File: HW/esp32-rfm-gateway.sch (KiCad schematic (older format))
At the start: 46 parts, among them J1 PinsI2C, J2 PinDbg, J20 MicroUSB-B, J3 PinsGP, J30 Ant, Q20 IRLML2244, SW1 BootBtn, U1 ESP-WROOM-32, U2 BD48K30, U20 MCP73831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

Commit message: Positions the components, almost ...
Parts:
- removed BT1: LiIon, CalinConnectors:BattHolder-AA-PCB, symbol calin:BATTERY
- removed J20: MicroUSB-B, CalinConnectors:USB-MicroB-10118194-0x0, symbol calin:MicroUSB-B
- removed J3: PinsGP, CalinConnectors:Pin_Header_Straight_1x07, symbol calin:CS_7
- removed J30: Ant, CalinConnectors:U.FL, symbol calin:CS_4
- removed SW1: BootBtn, CalinGeneric:SW-Push-4, symbol calin:SW-Push4
- added C5: 100nF, CalinGeneric:C0805HS, symbol Device:C
- added H3, H4: Hole, CalinGeneric:HoleNPT-M3, symbol calin:Hole
- added J1: Res, CalinConnectors:Pin_Header_Straight_1x02, symbol calin:CS_2
- added J2: Boot, CalinConnectors:Pin_Header_Straight_1x02, symbol calin:CS_2
- added J20: 220 V~, CalinConnectors:DG301-5-2, symbol calin:CS_2s
- added J21: c5V, CalinConnectors:Pin_Header_Straight_1x02, symbol calin:CS_2s
- added J22: s14500, CalinConnectors:BattHolder-AA-PCB, symbol calin:CS_2
- added J23: s18650, CalinConnectors:KEYS-1043, symbol calin:CS_2
- added J30: AntSMA, CalinConnectors:SMA-90, symbol calin:CS_5
- added SYM3: High Voltage !, Symbol:Symbol_HighVoltage_Type1_CopperTop_Big, symbol calin:Symbol_Generic
- added U24: IRM-05, CalinGeneric:IRM222A, symbol calin:IRM-05
- J3: renamed from J2; footprint CalinConnectors:Pin_Header_Straight_1x03 -> CalinConnectors:Pin_Header_Straight_1x03_Cyan
- renumbered J1 to J4
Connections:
- wire segments 195 -> 196
- no-connect marks 14 -> 22
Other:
- note removed: "1. Doar cu G738/G706: IRM-10-5 ca sursa de alimentare, dispare conectorul microUSB, sau pur si simplu ramane ca optional !\n2. Suport pt baterie 18650\n3. Modulul ESP32 trebuie in dreapta sus cum e in PCB acum !"
- moved on the sheet: C1, C20, C21, D20, R20, R21, U20

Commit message: Changes NPTH holes and adds 3 pin AC connector
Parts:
- removed J20: 220 V~, CalinConnectors:DG301-5-2, symbol calin:CS_2s
- added J20: 220V~, CalinConnectors:DG301-5-3, symbol calin:CS_3
- H1, H2, H3, H4: footprint CalinGeneric:HoleNPT-M3 -> CalinGeneric:HoleNPT-M2.5
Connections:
- net labels added: ACE, ACL, ACN, Earth
- wire segments 196 -> 194
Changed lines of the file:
@@
 F 0 "H1" H 10128 850 60  0000 L CNN
 F 1 "Hole" H 10150 800 60  0001 C CNN
-F 2 "CalinGeneric:HoleNPT-M3" H 10050 850 60  0001 C CNN
+F 2 "CalinGeneric:HoleNPT-M2.5" H 10050 850 60  0001 C CNN
 F 3 "" H 10050 850 60  0000 C CNN
 	1    10050 850
@@
 F 0 "H2" H 10628 850 60  0000 L CNN
 F 1 "Hole" H 10650 800 60  0001 C CNN
-F 2 "CalinGeneric:HoleNPT-M3" H 10550 850 60  0001 C CNN
+F 2 "CalinGeneric:HoleNPT-M2.5" H 10550 850 60  0001 C CNN
 F 3 "" H 10550 850 60  0000 C CNN
 	1    10550 850
@@
 PwrSW
 $Comp
-L calin:CS_2s J20
-U 1 1 5CAC0659
-P 1250 6850
-F 0 "J20" V 1350 6850 60  0000 C CNN
-F 1 "220 V~" H 1250 7000 50  0000 C CNN
-F 2 "CalinConnectors:DG301-5-2" H 1250 6900 60  0001 C CNN
-F 3 "" H 1250 6900 60  0000 C CNN
-	1    1250 6850
-	-1   0    0    -1
-$EndComp
-$Comp
 L calin:IRM-05 U24
 U 1 1 5CACF244
@@
 Wire Wire Line
 	2500 6950 2400 6950
-Wire Wire Line
-	1400 6800 1500 6800
-Wire Wire Line
-	1500 6800 1500 6750
-Wire Wire Line
-	1500 6750 1600 6750
-Wire Wire Line
-	1400 6900 1500 6900
-Wire Wire Line
-	1500 6900 1500 6950
-Wire Wire Line
-	1500 6950 1600 6950
 $Comp
 L calin:CS_2s J21
@@
 L calin:Symbol_Generic SYM3
 U 1 1 5CB3E766
-P 1050 6550
-F 0 "SYM3" H 1200 6550 50  0001 C CNN
-F 1 "High Voltage !" H 1128 6550 50  0000 L CNN
-F 2 "Symbol:Symbol_HighVoltage_Type1_CopperTop_Big" H 1050 6550 50  0001 C CNN
-F 3 "" V 1050 6550 50  0001 C CNN
-	1    1050 6550
+P 1050 6350
+F 0 "SYM3" H 1200 6350 50  0001 C CNN
+F 1 "High Voltage !" H 1128 6350 50  0000 L CNN
+F 2 "Symbol:Symbol_HighVoltage_Type1_CopperTop_Big" H 1050 6350 50  0001 C CNN
+F 3 "" V 1050 6350 50  0001 C CNN
+	1    1050 6350
 	1    0    0    -1
 $EndComp
@@
 F 0 "H3" H 10128 1050 60  0000 L CNN
 F 1 "Hole" H 10150 1000 60  0001 C CNN
-F 2 "CalinGeneric:HoleNPT-M3" H 10050 1050 60  0001 C CNN
+F 2 "CalinGeneric:HoleNPT-M2.5" H 10050 1050 60  0001 C CNN
 F 3 "" H 10050 1050 60  0000 C CNN
 	1    10050 1050
@@
 F 0 "H4" H 10628 1050 60  0000 L CNN
 F 1 "Hole" H 10650 1000 60  0001 C CNN
-F 2 "CalinGeneric:HoleNPT-M3" H 10550 1050 60  0001 C CNN
+F 2 "CalinGeneric:HoleNPT-M2.5" H 10550 1050 60  0001 C CNN
 F 3 "" H 10550 1050 60  0000 C CNN
 	1    10550 1050
@@
 	5750 5400 5750 4900
 Connection ~ 5750 5400
+$Comp
+L calin:CS_3 J20
+U 1 1 5CAC2EE6
+P 1050 6850
+F 0 "J20" V 1150 6850 60  0000 C CNN
+F 1 "220V~" H 1050 6650 50  0000 C CNN
+F 2 "CalinConnectors:DG301-5-3" H 1050 6950 60  0001 C CNN
+F 3 "" H 1050 6950 60  0000 C CNN
+	1    1050 6850
+	-1   0    0    1
+$EndComp
+$Comp
+L power:Earth #PWR0141
+U 1 1 5CAEA74F
+P 1500 7050
+F 0 "#PWR0141" H 1500 6800 50  0001 C CNN
+F 1 "Earth" H 1500 6900 50  0001 C CNN
+F 2 "" H 1500 7050 50  0001 C CNN
+F 3 "~" H 1500 7050 50  0001 C CNN
+	1    1500 7050
+	1    0    0    -1
+$EndComp
+Wire Wire Line
+	1200 6750 1600 6750
+Wire Wire Line
+	1200 6950 1600 6950
+Wire Wire Line
+	1500 6850 1500 7050
+Wire Wire Line
+	1200 6850 1500 6850
+Text Label 1250 6750 0    50   ~ 0
+ACL
+Text Label 1250 6850 0    50   ~ 0
+ACE
+Text Label 1250 6950 0    50   ~ 0
+ACN
 $EndSCHEMATC

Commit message: Creates an Earth plane
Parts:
- SYM3: footprint Symbol:Symbol_HighVoltage_Type1_CopperTop_Big -> Symbol:Symbol_Highvoltage_Type2_CopperTop_Small
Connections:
- net labels removed: ACE
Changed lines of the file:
@@
 Title "ESP32 RFM69/RFM9x Gateway"
 Date "2019-04-08"
-Rev "6"
+Rev "7"
 Comp "Calin Radoni"
 Comment1 ""
@@
 F 0 "SYM3" H 1200 6350 50  0001 C CNN
 F 1 "High Voltage !" H 1128 6350 50  0000 L CNN
-F 2 "Symbol:Symbol_HighVoltage_Type1_CopperTop_Big" H 1050 6350 50  0001 C CNN
+F 2 "Symbol:Symbol_Highvoltage_Type2_CopperTop_Small" H 1050 6350 50  0001 C CNN
 F 3 "" V 1050 6350 50  0001 C CNN
 	1    1050 6350
@@
 	-1   0    0    1
 $EndComp
+Wire Wire Line
+	1200 6750 1600 6750
+Wire Wire Line
+	1200 6950 1600 6950
+Wire Wire Line
+	1500 6850 1500 7050
+Wire Wire Line
+	1200 6850 1500 6850
+Text Label 1300 6750 0    50   ~ 0
+ACL
+Text Label 1300 6950 0    50   ~ 0
+ACN
 $Comp
 L power:Earth #PWR0141
-U 1 1 5CAEA74F
+U 1 1 5CB3D39A
 P 1500 7050
 F 0 "#PWR0141" H 1500 6800 50  0001 C CNN
@@
 	1    0    0    -1
 $EndComp
-Wire Wire Line
-	1200 6750 1600 6750
-Wire Wire Line
-	1200 6950 1600 6950
-Wire Wire Line
-	1500 6850 1500 7050
-Wire Wire Line
-	1200 6850 1500 6850
-Text Label 1250 6750 0    50   ~ 0
-ACL
 Text Label 1250 6850 0    50   ~ 0
-ACE
-Text Label 1250 6950 0    50   ~ 0
-ACN
+Earth
 $EndSCHEMATC

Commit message: The layout is established
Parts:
- added J5: PinsI2C, CalinConnectors:Pin_Header_Straight_1x04, symbol calin:CS_4
- added SYM4: High Voltage !, Symbol:Symbol_HighVoltage_Type1_CopperTop_Big, symbol calin:Symbol_Generic
- SYM3: footprint Symbol:Symbol_Highvoltage_Type2_CopperTop_Small -> Symbol:Symbol_HighVoltage_Type1_CopperTop_Big
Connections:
- wire segments 194 -> 198
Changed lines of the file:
@@
 Sheet 1 1
 Title "ESP32 RFM69/RFM9x Gateway"
-Date "2019-04-08"
-Rev "7"
+Date "2019-04-09"
+Rev "9"
 Comp "Calin Radoni"
 Comment1 ""
@@
 F 0 "SYM3" H 1200 6350 50  0001 C CNN
 F 1 "High Voltage !" H 1128 6350 50  0000 L CNN
-F 2 "Symbol:Symbol_Highvoltage_Type2_CopperTop_Small" H 1050 6350 50  0001 C CNN
+F 2 "Symbol:Symbol_HighVoltage_Type1_CopperTop_Big" H 1050 6350 50  0001 C CNN
 F 3 "" V 1050 6350 50  0001 C CNN
 	1    1050 6350
@@
 Text Label 1250 6850 0    50   ~ 0
 Earth
+$Comp
+L calin:Symbol_Generic SYM4
+U 1 1 5CAC5E73
+P 1050 6500
+F 0 "SYM4" H 1200 6500 50  0001 C CNN
+F 1 "High Voltage !" H 1128 6500 50  0000 L CNN
+F 2 "Symbol:Symbol_HighVoltage_Type1_CopperTop_Big" H 1050 6500 50  0001 C CNN
+F 3 "" V 1050 6500 50  0001 C CNN
+	1    1050 6500
+	1    0    0    -1
+$EndComp
+$Comp
+L calin:CS_4 J5
+U 1 1 5CAE5A37
+P 8200 1100
+F 0 "J5" H 8200 1350 60  0000 C CNN
+F 1 "PinsI2C" V 8300 1100 50  0000 C CNN
+F 2 "CalinConnectors:Pin_Header_Straight_1x04" H 8200 1250 60  0001 C CNN
+F 3 "" H 8200 1250 60  0000 C CNN
+	1    8200 1100
+	1    0    0    -1
+$EndComp
+$Comp
+L power:GND #PWR0142
+U 1 1 5CAE5A3D
+P 7950 1050
+F 0 "#PWR0142" H 7950 800 50  0001 C CNN
+F 1 "GND" V 7950 850 50  0000 C CNN
+F 2 "" H 7950 1050 50  0000 C CNN
+F 3 "" H 7950 1050 50  0000 C CNN
+	1    7950 1050
+	0    1    1    0
+$EndComp
+$Comp
+L power:+3V3 #PWR0143
+U 1 1 5CAE5A43
+P 7950 950
+F 0 "#PWR0143" H 7950 800 50  0001 C CNN
+F 1 "+3V3" V 7950 1150 50  0000 C CNN
+F 2 "" H 7950 950 50  0000 C CNN
+F 3 "" H 7950 950 50  0000 C CNN
+	1    7950 950
+	0    -1   -1   0
+$EndComp
+Wire Wire Line
+	8050 950  7950 950
+Wire Wire Line
+	8050 1050 7950 1050
+Wire Wire Line
+	8050 1150 7550 1150
+Wire Wire Line
+	8050 1250 7550 1250
+Text Label 7650 1150 0    50   ~ 0
+SCL
+Text Label 7650 1250 0    50   ~ 0
+SDA
 $EndSCHEMATC

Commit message: The margins are established
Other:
- note added: "1. MCP73832T-2ACI (sau 2ADI) pentru ca are Stat open-drain\n2. Split R25 ca sa vezi daca 5V e prezenta sau NU"
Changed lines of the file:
@@
 Text Label 7650 1250 0    50   ~ 0
 SDA
+Text Notes 4300 4200 0    118  ~ 0
+1. MCP73832T-2ACI (sau 2ADI) pentru ca are Stat open-drain\n2. Split R25 ca sa vezi daca 5V e prezenta sau NU
 $EndSCHEMATC

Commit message: Changes the power supply to provide stats, to a better annotation and to comply with ERC checks
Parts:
- added R26: 10k, CalinGeneric:R0805HS, symbol calin:R
- R21: value 1K -> 330
- U21: renamed from U20; value MCP73831 -> MCP73832T-2ACI
- renumbered R26 to R27, R27 to R28, U24 to U20, U21 to U24
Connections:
- net labels added: ADC_Vin, ChargeStat
- net labels removed: ADCIN, VinBOR
- wire segments 198 -> 207
- no-connect marks 22 -> 21
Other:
- note removed: "1. MCP73832T-2ACI (sau 2ADI) pentru ca are Stat open-drain\n2. Split R25 ca sa vezi daca 5V e prezenta sau NU"
- moved on the sheet: C22, C23, C24, C5, D21, J21, L21, Q20, R22, R23, R24, R25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

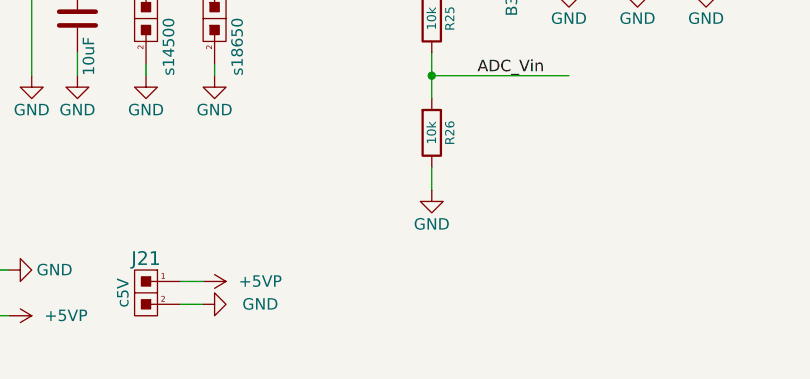
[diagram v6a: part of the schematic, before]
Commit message: Adds a new 5V header to be placed as placeholder in the power section
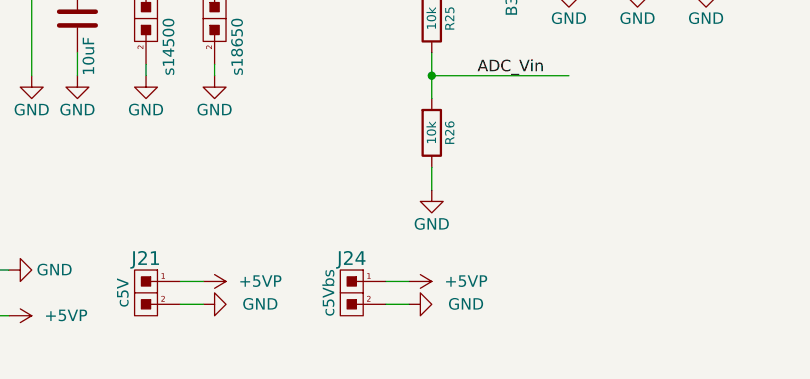
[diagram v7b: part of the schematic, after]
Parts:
- added J24: c5Vbs, CalinConnectors:Pin_Header_Angled_1x02, symbol calin:CS_2s
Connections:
- wire segments 207 -> 209
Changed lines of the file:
@@
 Sheet 1 1
 Title "ESP32 RFM69/RFM9x Gateway"
-Date "2019-04-09"
-Rev "9"
+Date "2019-04-13"
+Rev "10"
 Comp "Calin Radoni"
 Comment1 ""
@@
 	6450 4900 5600 4900
 $Comp
-L power:PWR_FLAG #FLG?
+L power:PWR_FLAG #FLG0104
 U 1 1 5CC8F59E
 P 1550 6850
-F 0 "#FLG?" H 1550 6925 50  0001 C CNN
+F 0 "#FLG0104" H 1550 6925 50  0001 C CNN
 F 1 "PWR_FLAG" V 1500 6950 20  0000 C CNN
 F 2 "" H 1550 6850 50  0001 C CNN
@@
 	1550 6850 1500 6850
 Connection ~ 1500 6850
+$Comp
+L calin:CS_2s J24
+U 1 1 5CB25633
+P 4050 6850
+F 0 "J24" H 4050 7000 60  0000 C CNN
+F 1 "c5Vbs" V 4150 6850 50  0000 C CNN
+F 2 "CalinConnectors:Pin_Header_Angled_1x02" H 4050 6900 60  0001 C CNN
+F 3 "" H 4050 6900 60  0000 C CNN
+	1    4050 6850
+	-1   0    0    -1
+$EndComp
+$Comp
+L power:+5VP #PWR0144
+U 1 1 5CB25639
+P 4300 6800
+F 0 "#PWR0144" H 4300 6650 50  0001 C CNN
+F 1 "+5VP" V 4300 7050 50  0000 C CNN
+F 2 "" H 4300 6800 50  0000 C CNN
+F 3 "" H 4300 6800 50  0000 C CNN
+	1    4300 6800
+	0    1    1    0
+$EndComp
+$Comp
+L power:GND #PWR0145
+U 1 1 5CB2563F
+P 4300 6900
+F 0 "#PWR0145" H 4300 6650 50  0001 C CNN
+F 1 "GND" V 4300 6650 50  0000 C CNN
+F 2 "" H 4300 6900 50  0000 C CNN
+F 3 "" H 4300 6900 50  0000 C CNN
+	1    4300 6900
+	0    -1   -1   0
+$EndComp
+Wire Wire Line
+	4300 6800 4200 6800
+Wire Wire Line
+	4200 6900 4300 6900
 $EndSCHEMATC

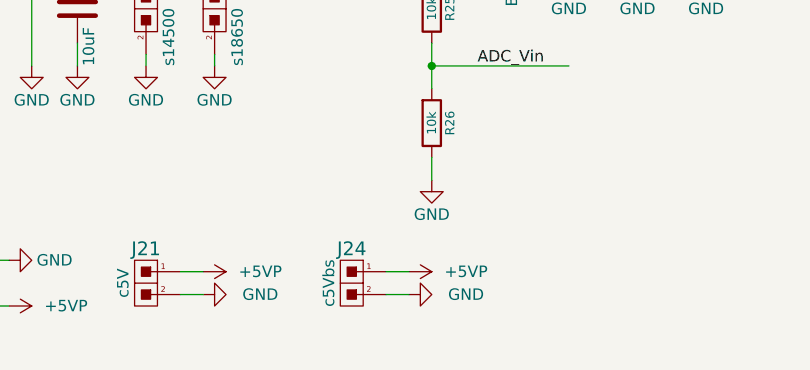
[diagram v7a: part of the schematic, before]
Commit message: Changes the 5V header from power section to include VBatt
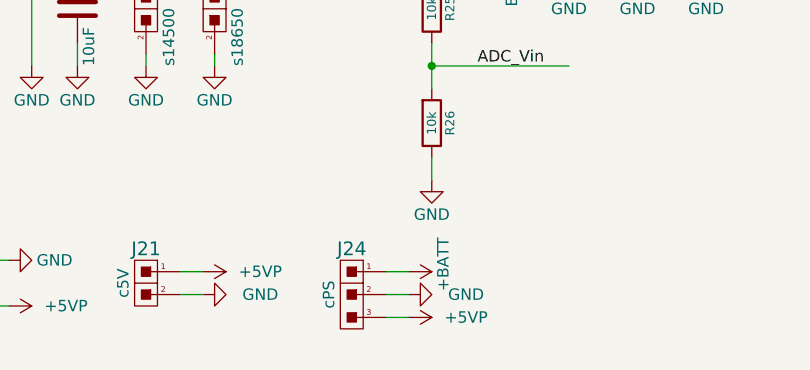
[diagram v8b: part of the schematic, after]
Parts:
- removed J24: c5Vbs, CalinConnectors:Pin_Header_Angled_1x02, symbol calin:CS_2s
- added J24: cPS, CalinConnectors:Pin_Header_Angled_1x03, symbol calin:CS_3
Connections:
- wire segments 209 -> 210
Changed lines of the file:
@@
 Title "ESP32 RFM69/RFM9x Gateway"
 Date "2019-04-13"
-Rev "10"
+Rev "11"
 Comp "Calin Radoni"
 Comment1 ""
@@
 Connection ~ 1500 6850
 $Comp
-L calin:CS_2s J24
-U 1 1 5CB25633
-P 4050 6850
-F 0 "J24" H 4050 7000 60  0000 C CNN
-F 1 "c5Vbs" V 4150 6850 50  0000 C CNN
-F 2 "CalinConnectors:Pin_Header_Angled_1x02" H 4050 6900 60  0001 C CNN
-F 3 "" H 4050 6900 60  0000 C CNN
-	1    4050 6850
-	-1   0    0    -1
-$EndComp
-$Comp
 L power:+5VP #PWR0144
 U 1 1 5CB25639
-P 4300 6800
-F 0 "#PWR0144" H 4300 6650 50  0001 C CNN
-F 1 "+5VP" V 4300 7050 50  0000 C CNN
-F 2 "" H 4300 6800 50  0000 C CNN
-F 3 "" H 4300 6800 50  0000 C CNN
-	1    4300 6800
+P 4300 7000
+F 0 "#PWR0144" H 4300 6850 50  0001 C CNN
+F 1 "+5VP" V 4300 7250 50  0000 C CNN
+F 2 "" H 4300 7000 50  0000 C CNN
+F 3 "" H 4300 7000 50  0000 C CNN
+	1    4300 7000
 	0    1    1    0
 $EndComp
@@
 $EndComp
 Wire Wire Line
-	4300 6800 4200 6800
-Wire Wire Line
 	4200 6900 4300 6900
+$Comp
+L calin:CS_3 J24
+U 1 1 5CB26001
+P 4050 6900
+F 0 "J24" H 4050 7100 60  0000 C CNN
+F 1 "cPS" V 4150 6900 50  0000 C CNN
+F 2 "CalinConnectors:Pin_Header_Angled_1x03" H 4050 7000 60  0001 C CNN
+F 3 "" H 4050 7000 60  0000 C CNN
+	1    4050 6900
+	-1   0    0    -1
+$EndComp
+$Comp
+L power:+BATT #PWR0146
+U 1 1 5CB3D514
+P 4300 6800
+F 0 "#PWR0146" H 4300 6650 50  0001 C CNN
+F 1 "+BATT" H 4150 6950 50  0000 L CNN
+F 2 "" H 4300 6800 50  0001 C CNN
+F 3 "" H 4300 6800 50  0001 C CNN
+	1    4300 6800
+	0    1    1    0
+$EndComp
+Wire Wire Line
+	4200 6800 4300 6800
+Wire Wire Line
+	4200 7000 4300 7000
 $EndSCHEMATC
